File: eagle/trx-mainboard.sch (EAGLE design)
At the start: 36 parts, among them J1 629722000214, J2 DF12NB(3.0)-10DP-0.5V, P1 S2B-PH-SM4-TB, Q1 BSS84

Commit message: Added basic auto-route
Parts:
- removed U$7: BC034-04-A-V-0150-L-C, con-gct:BC034-04-A-V-0150-L-C
- removed U$8: BC075-04-A-L-A, con-gct:BC075-04-A-L-A
- added JP1: (no value), pinhead2:PINHD-1X04_2.54-SMD
- added U$11: BG230-04, con-gct:BG230-04
- added U$12: BG035-04, con-gct:BG035-04
- renumbered U$3 to U2
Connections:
- net +3V3: now also JP1.1
- net GND: now also JP1.4, U$11.1; no longer U$8.1
- net SWCLK: now also JP1.3
- net SWDIO: now also JP1.2
- net USB_D+: now also U$12.3; no longer U$7.3
- net USB_D-: now also U$12.2; no longer U$7.2
- net USB_DM: now also U$11.2; no longer U$8.2
- net USB_DP: now also U$11.3; no longer U$8.3
- net USB_GND: now also U$12.1; no longer U$7.1
- net USB_V: now also U$12.4; no longer U$7.4
- net VUSB: now also U$11.4; no longer U$8.4

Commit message: Finalized alpha design
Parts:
- removed U$12: BG035-04, con-gct:BG035-04
- added R7: 33R, rcl:R-EU_R0805
- added U$3: BG080-04, con-gct:BG080-04
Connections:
- removed net LED_RGB_B: J2.7
- removed net LED_RGB_G: J2.5
- removed net LED_RGB_R: J2.3
- new net LED_D: J2.3, R7.1
- net +3V3: now also J2.1, U$10.VDDIO2
- net GND: now also U$2.AGND, U$2.FB, U$2.PGND
- net N$10: now also R7.2, U$10.PB4; no longer U$2.AGND, U$2.FB, U$2.PGND
- net N$9: now also Q1.S; no longer Q1.D
- net USB_D+: now also U$3.3; no longer U$12.3
- net USB_D-: now also U$3.2; no longer U$12.2
- net USB_GND: now also U$3.1; no longer U$12.1
- net USB_V: now also U$3.4; no longer U$12.4
- net V+: now also Q1.D; no longer Q1.S
- net VBAT+: no longer J2.1

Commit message: Added new layout and gerber files
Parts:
- C11: value 100nF -> 10uF
- C12: value 100nF -> 3.3nF
- R4: value 3k -> 1.8k
- R5: value 3k -> 10k
- R6: value 3k -> 100k
- renumbered U$6 to LORA2, U$9 to LORA1
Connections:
- net USB_GND: now also U$3.4; no longer U$3.1
- net USB_V: now also U$3.1; no longer U$3.4
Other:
- note added: "2.2uH"

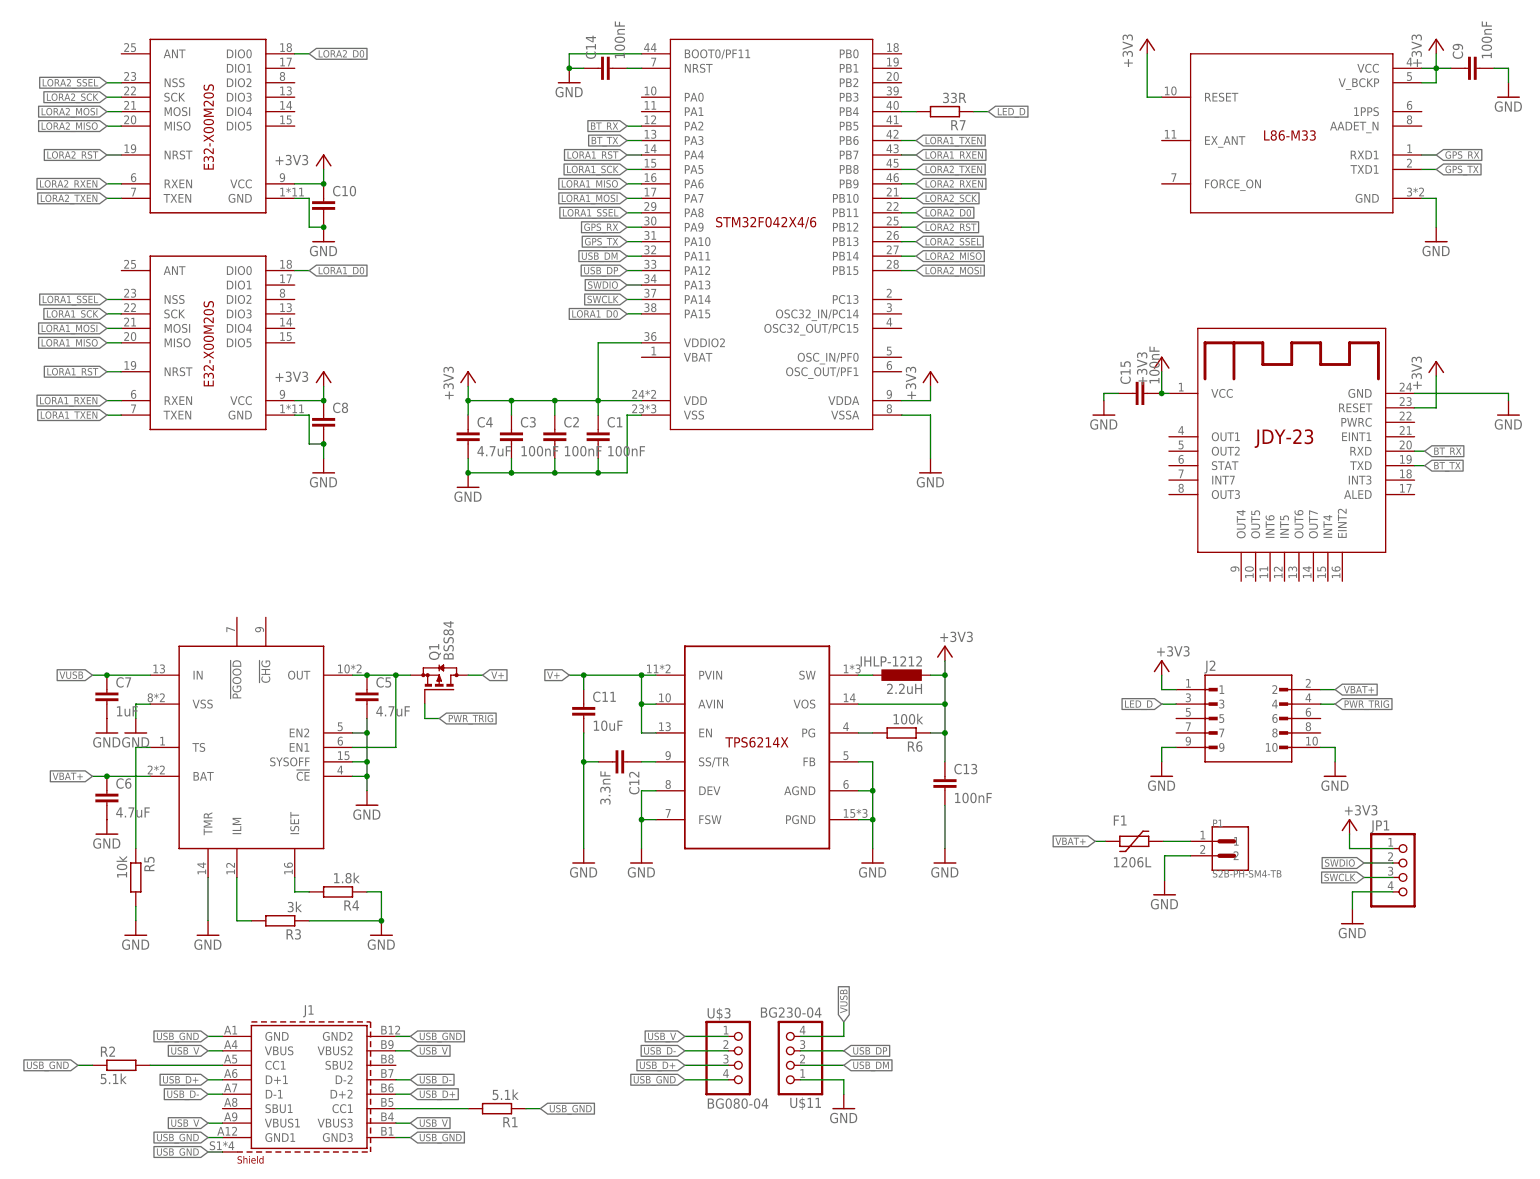
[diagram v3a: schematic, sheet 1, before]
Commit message: Designed new boards wit fixed errors
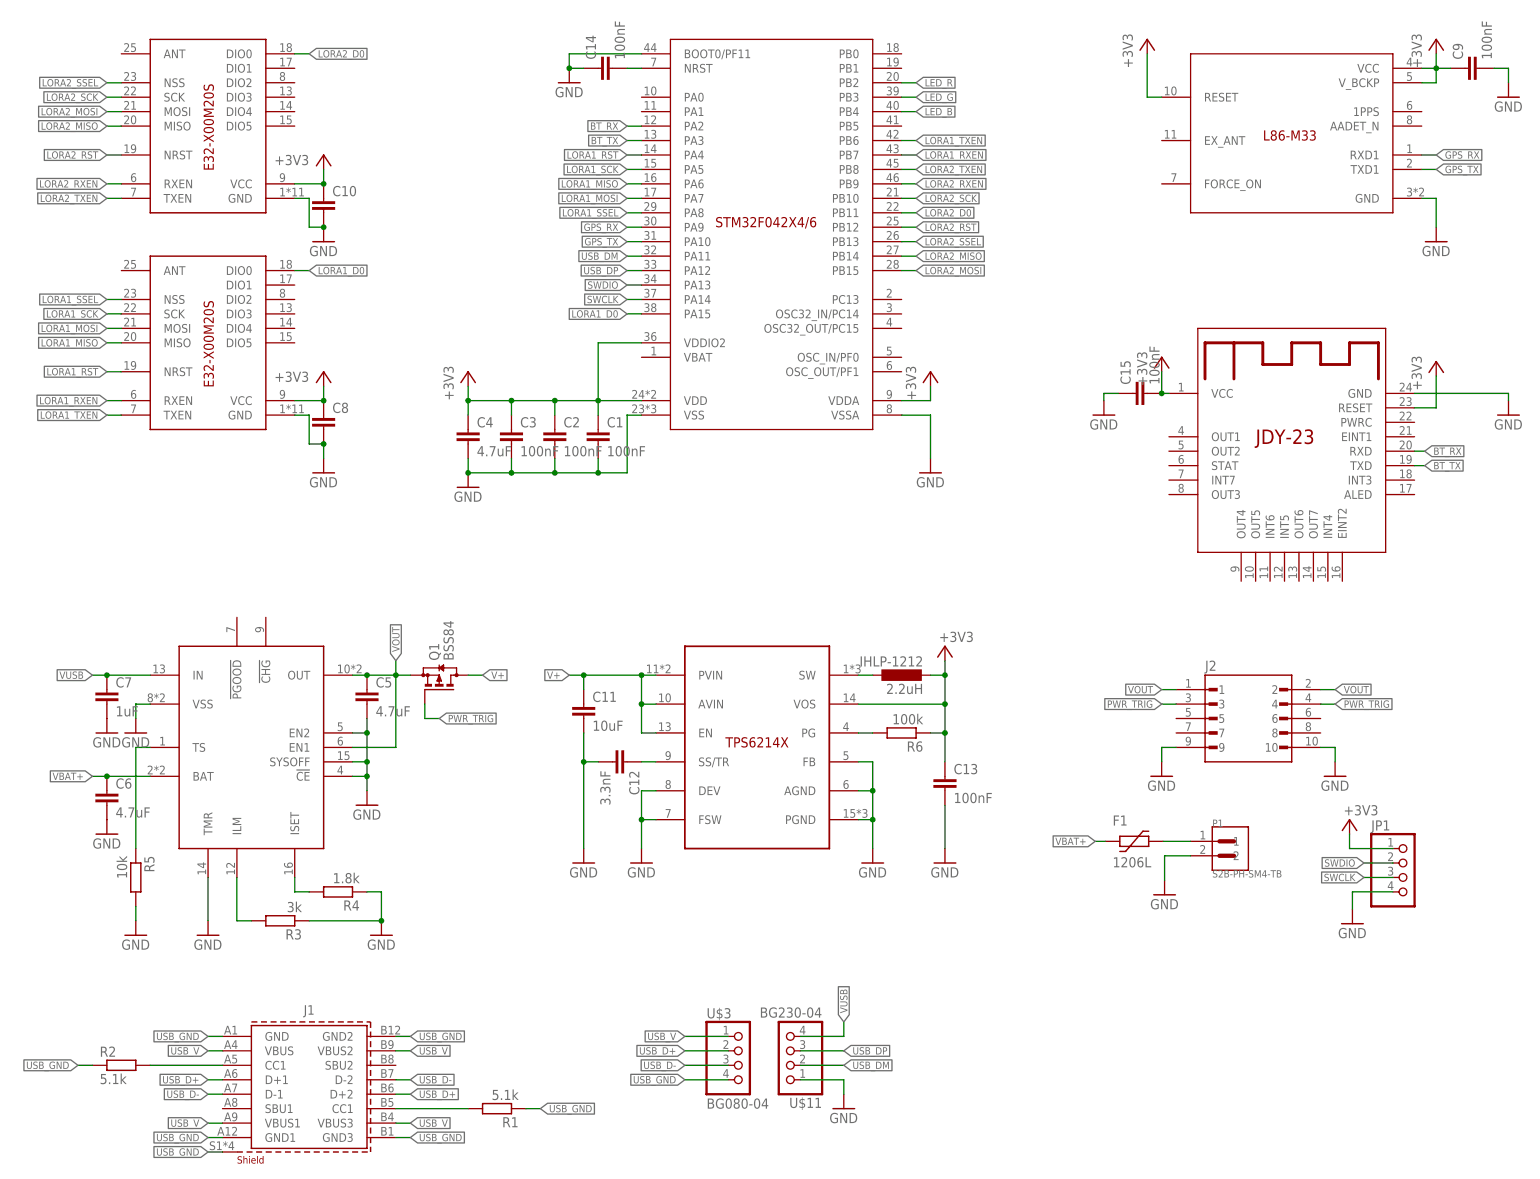
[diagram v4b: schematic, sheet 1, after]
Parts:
- removed R7: 33R, rcl:R-EU_R0805
- added Q2, Q3, Q4: BSS123, transistor-small-signal:BSS123
- added R10, R11, R8, R9: (no value), rcl:R-EU_R0805
- added U$12, U$13, U$6, U$7, U$8, U$9: RGB_LED, led:RGB_LED
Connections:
- removed net LED_D: J2.3, R7.1
- removed net N$10: R7.2, U$10.PB4
- removed net N$9: C5.1, Q1.S, U2.EN1, U2.OUT
- new net CAT_B: Q4.D, U$12.C.B, U$13.C.B, U$6.C.B, U$7.C.B, U$8.C.B, U$9.C.B
- new net CAT_G: Q2.D, U$12.C.G, U$13.C.G, U$6.C.G, U$7.C.G, U$8.C.G, U$9.C.G
- new net CAT_R: Q3.D, U$12.C.R, U$13.C.R, U$6.C.R, U$7.C.R, U$8.C.R, U$9.C.R
- new net LED_B: R10.2, U$10.PB4
- new net LED_G: R9.2, U$10.PB3
- new net LED_R: R11.2, U$10.PB2
- new net N$13: Q2.G, R9.1
- new net N$14: Q3.S, R8.2
- new net N$16: Q4.G, R10.1
- new net N$18: Q3.G, R11.1
- new net VOUT: C5.1, J2.1, J2.2, Q1.S, U2.EN1, U2.OUT
- net +3V3: now also U$12.A.B, U$12.A.G, U$12.A.R, U$13.A.B, U$13.A.G, U$13.A.R, U$6.A.B, U$6.A.G, U$6.A.R, U$7.A.B, U$7.A.G, U$7.A.R, U$8.A.B, U$8.A.G, U$8.A.R, U$9.A.B, U$9.A.G, U$9.A.R; no longer J2.1
- net GND: now also Q2.S, Q4.S, R8.1
- net PWR_TRIG: now also J2.3
- net USB_D+: now also U$3.2; no longer U$3.3
- net USB_D-: now also U$3.3; no longer U$3.2
- net VBAT+: no longer J2.2

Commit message: Modified board layout
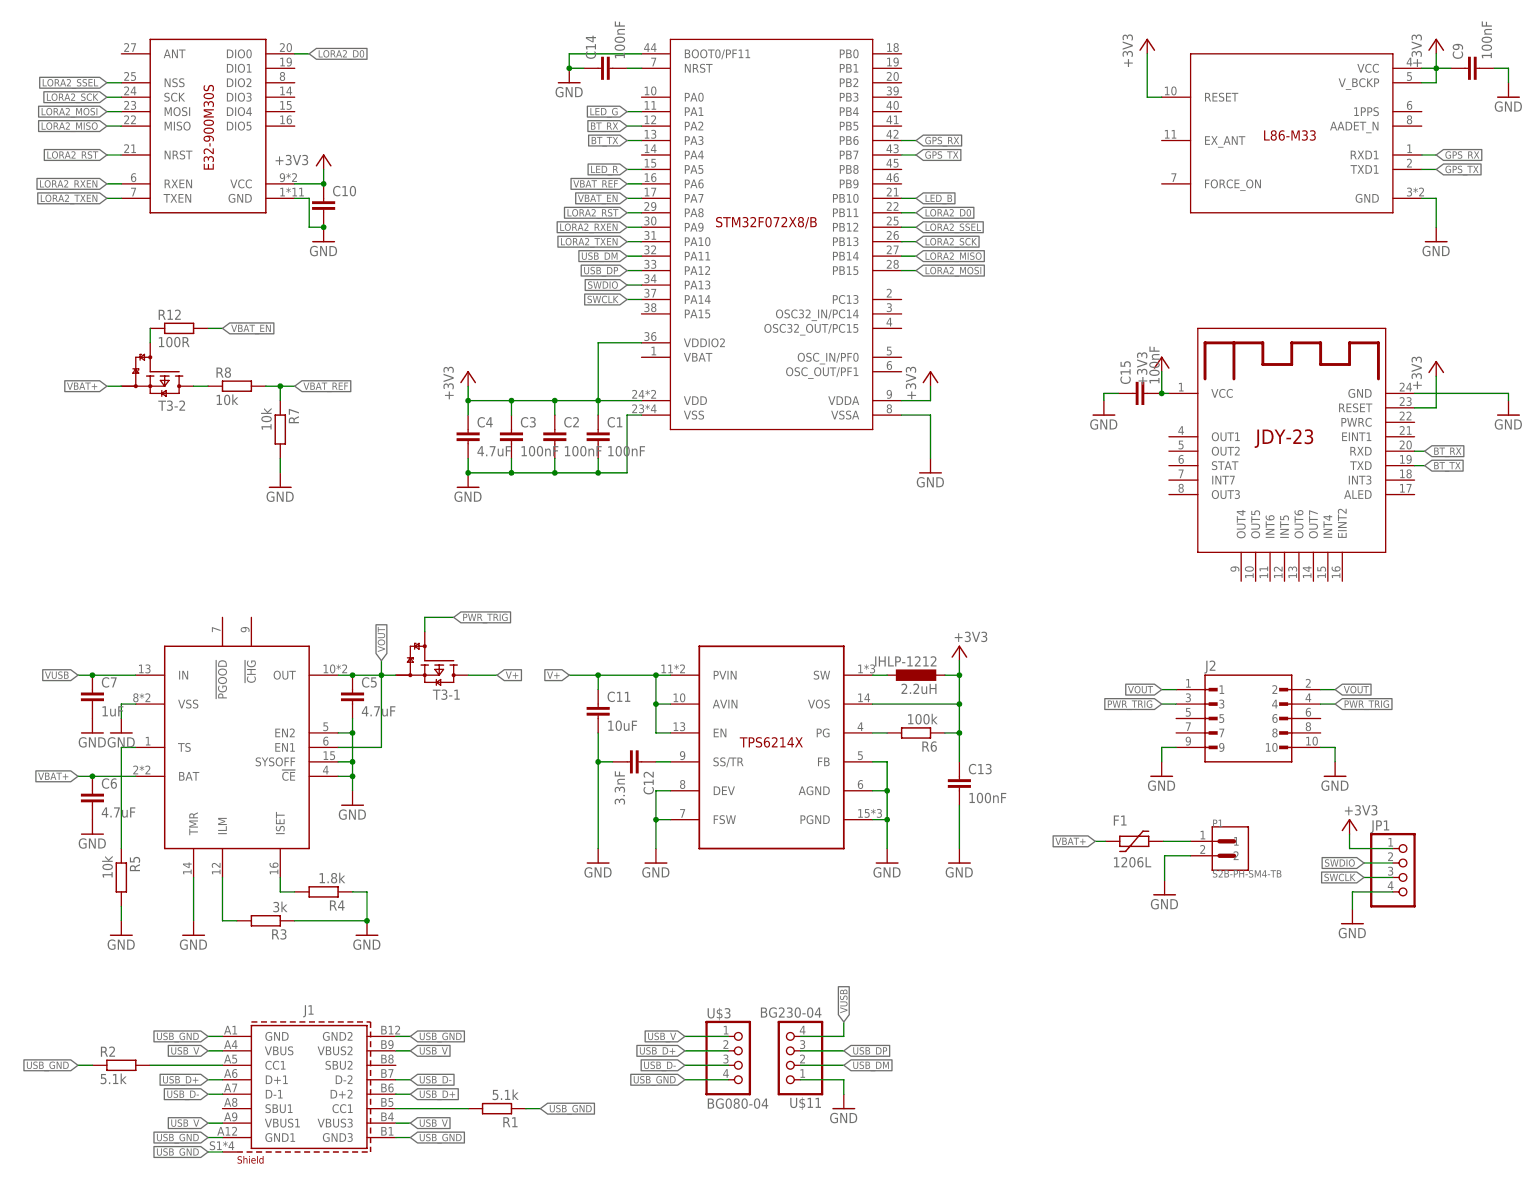
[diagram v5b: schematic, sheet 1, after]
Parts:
- removed C8: 4.7uF, rcl:C-EUC0805
- removed LORA1, LORA2: E32-X00M20S, ebyte:E32-X00M20S
- removed Q1: BSS84, transistor-small-signal:BSS84
- removed Q2, Q3, Q4: BSS123, transistor-small-signal:BSS123
- added R12: 100R, rcl:R-EU_R0805
- added R7: 10k, rcl:R-EU_R0805
- added T1, T2: NX3008NBKS, NXP_60_26022015:NX3008NBKS
- added T3: NX3008PBKS, NXP_60_26022015:NX3008PBKS
- added U$14: E32-900M30S, ebyte:E32-900M30S
- R10, R11, R9: value (none) -> 100R
- R8: value (none) -> 10k
- U$10: value STM32-F042X4/6-48 -> STM32-F072X8/B-48; device st-microelectronics:STM32-F042X4/6-48 -> st-microelectronics:STM32-F072X8/B-48
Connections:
- removed net LORA1_D0: LORA1.DIO0, U$10.PA15
- removed net LORA1_MISO: LORA1.MISO, U$10.PA6
- removed net LORA1_MOSI: LORA1.MOSI, U$10.PA7
- removed net LORA1_RST: LORA1.NRST, U$10.PA4
- removed net LORA1_RXEN: LORA1.RXEN, U$10.PB7
- removed net LORA1_SCK: LORA1.SCK, U$10.PA5
- removed net LORA1_SSEL: LORA1.NSS, U$10.PA8
- removed net LORA1_TXEN: LORA1.TXEN, U$10.PB6
- new net N$17: R12.1, T3-2.G
- new net VBAT_EN: R12.2, U$10.PA7
- new net VBAT_REF: R7.1, R8.2, U$10.PA6
- net +3V3: now also U$14.VCC; no longer C8.1, LORA1.VCC, LORA2.VCC
- net CAT_B: now also T1-2.D; no longer Q4.D
- net CAT_G: now also T1-1.D; no longer Q2.D
- net CAT_R: now also T2-1.D; no longer Q3.D
- net GND: now also R7.2, T1-1.S, T1-2.S, T2-1.S, U$14.GND; no longer C8.2, LORA1.GND, LORA2.GND, Q2.S, Q4.S, R8.1
- net GPS_RX: now also U$10.PB6; no longer U$10.PA9
- net GPS_TX: now also U$10.PB7; no longer U$10.PA10
- net LED_B: now also U$10.PB10; no longer U$10.PB4
- net LED_G: now also U$10.PA1; no longer U$10.PB3
- net LED_R: now also U$10.PA5; no longer U$10.PB2
- net LORA2_D0: now also U$14.DIO0; no longer LORA2.DIO0
- net LORA2_MISO: now also U$14.MISO; no longer LORA2.MISO
- net LORA2_MOSI: now also U$14.MOSI; no longer LORA2.MOSI
- net LORA2_RST: now also U$10.PA8, U$14.NRST; no longer LORA2.NRST, U$10.PB12
- net LORA2_RXEN: now also U$10.PA9, U$14.RXEN; no longer LORA2.RXEN, U$10.PB9
- net LORA2_SCK: now also U$10.PB13, U$14.SCK; no longer LORA2.SCK, U$10.PB10
- net LORA2_SSEL: now also U$10.PB12, U$14.NSS; no longer LORA2.NSS, U$10.PB13
- net LORA2_TXEN: now also U$10.PA10, U$14.TXEN; no longer LORA2.TXEN, U$10.PB8
- net N$13: now also T1-1.G; no longer Q2.G
- net N$14: now also R8.1, T3-2.D; no longer Q3.S, R8.2
- net N$16: now also T1-2.G; no longer Q4.G
- net N$18: now also T2-1.G; no longer Q3.G
- net PWR_TRIG: now also T3-1.G; no longer Q1.G
- net V+: now also T3-1.D; no longer Q1.D
- net VBAT+: now also T3-2.S
- net VOUT: now also T3-1.S; no longer Q1.S
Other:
- moved on the sheet: C11, C12, C13, C5, C6, C7, R10, R11, R3, R4, R5, R6
